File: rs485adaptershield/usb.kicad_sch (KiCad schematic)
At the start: 0 parts

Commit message: more work
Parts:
- added C22, C23, C26: 100n, Capacitor_SMD:C_0603_1608Metric, symbol Device:C
- added C24, C25: 1u, Capacitor_SMD:C_0603_1608Metric, symbol Device:C
- added C4, C6: 100n, Capacitor_SMD:C_0402_1005Metric, symbol Device:C
- added IC1: USB2422-I_MJ, QFN50P400X400X100-25N-D, symbol USB2422-I_MJ:USB2422-I_MJ
- added J1, J5: (no value), Connector_USB:USB_C_Receptacle_GCT_USB4110, symbol Connector:USB_C_Receptacle_USB2.0_16P
- added R14, R15, R16, R9: 5.1k, Capacitor_SMD:C_0402_1005Metric, symbol Device:R
- added U8: AP2171W, Package_TO_SOT_SMD:SOT-23-5, symbol Power_Management:AP2171W
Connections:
- new net: C4.1, J1.SH (SHIELD)
- new net: C6.1, J5.SH (SHIELD)
- new net: J5.A4 (VBUS), J5.A9 (VBUS), J5.B4 (VBUS), J5.B9 (VBUS)
- new net: J1.A4 (VBUS), J1.A9 (VBUS), J1.B4 (VBUS), J1.B9 (VBUS)
- new net +3.3V: C22.2, C23.2, C24.2, IC1.1 (VDD33_1), IC1.18 (VDD33_3), IC1.9 (VDD33_2)
- new net CRFILT: C25.2, IC1.10 (CRFILT)
- new net DA+: J1.A6 (D+), J1.B6 (D+)
- new net DA-: J1.A7 (D-), J1.B7 (D-)
- new net DB+: J5.A6 (D+), J5.B6 (D+)
- new net DB-: J5.A7 (D-), J5.B7 (D-)
- new net GND: C22.1, C23.1, C24.1, C25.1, C26.1, C4.2, C6.2, J1.A1 (GND), J1.A12 (GND), J1.B1 (GND), J1.B12 (GND), J5.A1 (GND), J5.A12 (GND), J5.B1 (GND), J5.B12 (GND), R14.2, R15.2, R16.2, R9.2
- new net PLLFILT: C26.2
- new net USB_CC1A: J1.A5 (CC1), R9.1
- new net USB_CC1B: J5.A5 (CC1), R15.1
- new net USB_CC2A: J1.B5 (CC2), R14.1
- new net USB_CC2B: J5.B5 (CC2), R16.1
- no-connect marks 0 -> 5
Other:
- note added: "1A MAX Silkscreen"
- note added: "pin 1"
- note added: "pin 10"
- note added: "pin 18"
- note added: "pin 23"
- note added: "pin 9"

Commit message: more progress
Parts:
- removed R9: 5.1k, Capacitor_SMD:C_0402_1005Metric, symbol Device:R
- added C27, C28, C29, C30, C33: 100n, Capacitor_SMD:C_0603_1608Metric, symbol Device:C
- added C31, C32: 9n, Capacitor_SMD:C_0603_1608Metric, symbol Device:C
- added D4, D6: LED, LED_SMD:LED_0805_2012Metric, symbol Device:LED
- added R10, R29: 560, Resistor_SMD:R_0805_2012Metric, symbol Device:R
- added R23: 22k, Capacitor_SMD:C_0402_1005Metric, symbol Device:R
- added R26: 12k, Capacitor_SMD:C_0402_1005Metric, symbol Device:R
- added R27, R28: 100k, Capacitor_SMD:C_0402_1005Metric, symbol Device:R
- added R30: 1k, Capacitor_SMD:C_0402_1005Metric, symbol Device:R
- added R31: 2k, Capacitor_SMD:C_0402_1005Metric, symbol Device:R
- added U9: AP2171W, Package_TO_SOT_SMD:SOT-23-5, symbol Power_Management:AP2171W
- added U901, U902: USBLC6-2SC6, Package_TO_SOT_SMD:SOT-23-6, symbol Power_Protection:USBLC6-2SC6
- added Y1: XRCGB24M000F1SBJR0, symbol Device:Crystal
- R14, R15, R16: value 5.1k -> 22k
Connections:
- net PLLFILT is gone; now on net PLL_FILTER: C26.2
- net +3.3V: now also IC1.16 (VBUS_DET), R27.1
- net DA+: now also IC1.3 (USBDP_DN1/PRT_DIS_P1), U901.4 (I/O2); no longer J1.A6 (D+), J1.B6 (D+)
- net DA-: now also IC1.2 (USBDM_DN1/PRT_DIS_M1), U901.6 (I/O1); no longer J1.A7 (D-), J1.B7 (D-)
- net DB+: now also IC1.5 (USBDP_DN2/PRT_DIS_P2), U902.4 (I/O2); no longer J5.A6 (D+), J5.B6 (D+)
- net DB-: now also IC1.4 (USBDM_DN2/PRT_DIS_M2), U902.6 (I/O1); no longer J5.A7 (D-), J5.B7 (D-)
- net GND: now also IC1.25 (EP), U8.2 (GND), C27.1, C28.1, C29.1, C30.1, C31.1, C32.1, C33.1, D4.1 (K), D6.1 (K), R26.2, R28.2, R31.2, U9.2 (GND), U901.2 (GND), U902.2 (GND); no longer R14.2, R15.2, R16.2
- net USB_CC1A: now also R15.1
- net USB_CC1B: now also R23.1; no longer R15.1
- net VBUS_OUT_A: now reaches U8.1 (OUT)
- net VBUS_OUT_A: now also J1.A4 (VBUS), J1.A9 (VBUS), J1.B4 (VBUS), J1.B9 (VBUS), C27.2, R10.1, U901.5 (VBUS)
- net ¬FLG_A: now reaches U8.3 (~{FLG})
- net ¬FLG_A: now also IC1.8 (OCS1_N)
- net EN_A: now reaches U8.4 (EN)
- net EN_A: now also IC1.7 (PRTPWR1/(BC_EN1))
- net VUSB1: now reaches U8.5 (IN)
- net VUSB1: now also R14.2, R15.2, C28.2
- net VBUS_OUT_B: now reaches J5.A4 (VBUS), J5.A9 (VBUS), J5.B4 (VBUS), J5.B9 (VBUS)
- net VBUS_OUT_B: now also C30.2, R29.1, U9.1 (OUT), U902.5 (VBUS)
- net EN_B: now reaches IC1.11 (PRTPWR2)
- net EN_B: now also U9.4 (EN)
- net ¬FLG_B: now reaches IC1.12 (OCS2_N)
- net ¬FLG_B: now also U9.3 (~{FLG})
- net CFG: now reaches IC1.14 (SMBCLK/CFG_SEL0)
- net CFG: now also R28.1
- net ¬RESET: now reaches IC1.15 (RESET_N)
- net ¬RESET: now also C33.2, R27.2, R30.2, R31.1
- net USB_D-: now reaches IC1.19 (USBDM_UP)
- net USB_D+: now reaches IC1.20 (USBDP_UP)
- net XTAL_2: now reaches IC1.21 (XTALOUT/(CLKIN_EN))
- net XTAL_2: now also C31.2, Y1.1
- net XTAL_1: now reaches IC1.22 (XTALIN/CLKIN)
- net XTAL_1: now also C32.2, Y1.2
- net PLL_FILTER: now reaches IC1.23 (PLLFILT)
- net RBIAS: now reaches IC1.24 (RBIAS)
- net RBIAS: now also R26.1
- new net: J1.A7 (D-), J1.B7 (D-), U901.1 (I/O1)
- new net: J1.A6 (D+), J1.B6 (D+), U901.3 (I/O2)
- new net: J5.A7 (D-), J5.B7 (D-), U902.1 (I/O1)
- new net: J5.A6 (D+), J5.B6 (D+), U902.3 (I/O2)
- new net: D4.2 (A), R10.2
- new net: D6.2 (A), R29.2
- new net VUSB2: C29.2, R16.2, R23.2, U9.5 (IN)
- new net ¬USB_HUB_RST: R30.1
- no-connect marks 5 -> 7
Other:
- note added: "1.5A MAX Silkscreen"
- note added: "precision"
- note removed: "1A MAX Silkscreen"
- moved on the sheet: C22, C23, C24, C25, C26, C4, C6, IC1, J1, J5, R14, U8

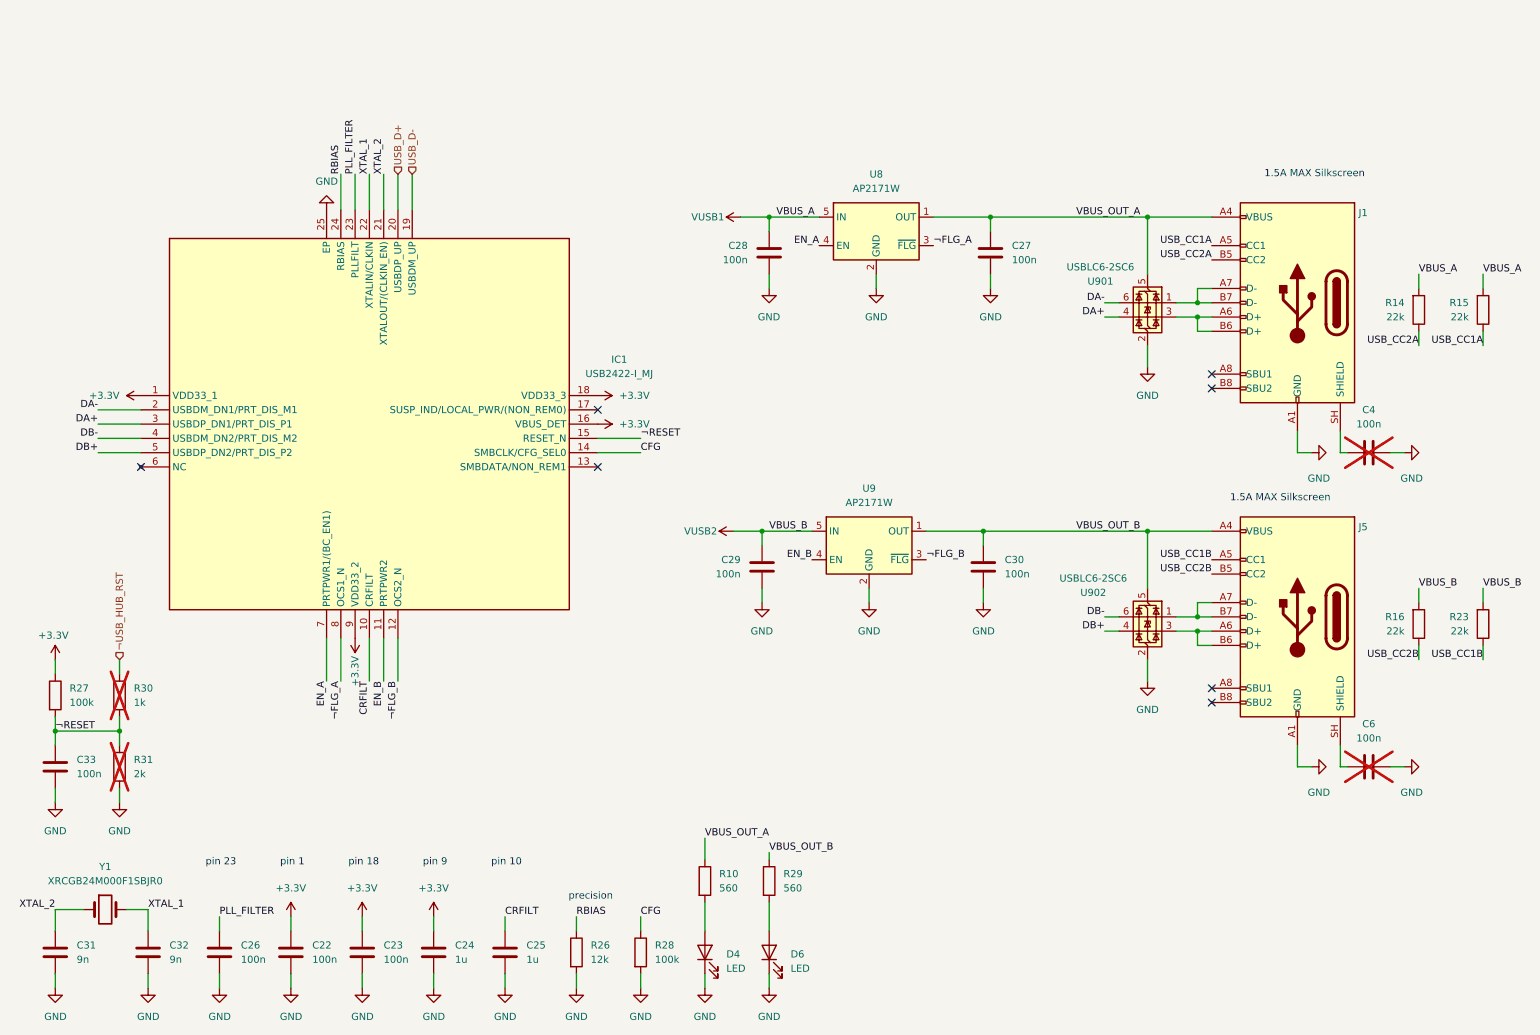
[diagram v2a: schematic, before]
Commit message: schematic mostly finished w/o footprints
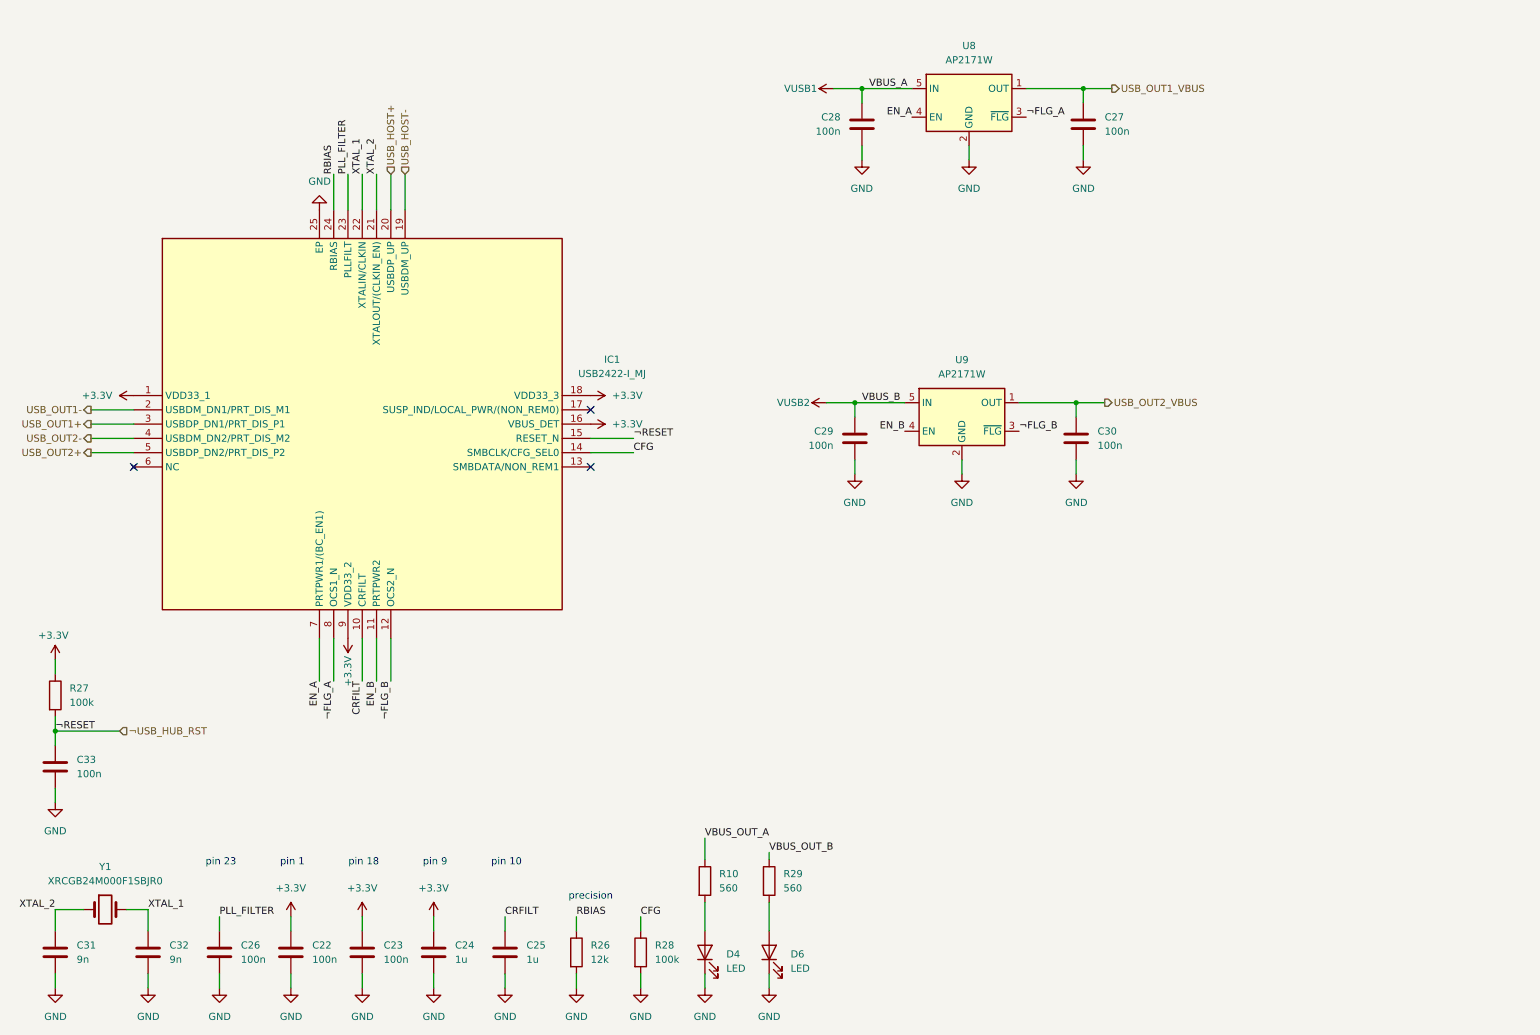
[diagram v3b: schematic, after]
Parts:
- removed C4, C6: 100n, Capacitor_SMD:C_0402_1005Metric, symbol Device:C
- removed J1, J5: (no value), Connector_USB:USB_C_Receptacle_GCT_USB4110, symbol Connector:USB_C_Receptacle_USB2.0_16P
- removed R14, R15, R16, R23: 22k, Capacitor_SMD:C_0402_1005Metric, symbol Device:R
- removed R30: 1k, Capacitor_SMD:C_0402_1005Metric, symbol Device:R
- removed R31: 2k, Capacitor_SMD:C_0402_1005Metric, symbol Device:R
- removed U901, U902: USBLC6-2SC6, Package_TO_SOT_SMD:SOT-23-6, symbol Power_Protection:USBLC6-2SC6
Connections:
- net ¬RESET is gone; now on net ¬USB_HUB_RST: C33.2, IC1.15 (RESET_N), R27.2
- net VBUS_OUT_A: no longer C27.2, U8.1 (OUT)
- net VBUS_OUT_B: no longer C30.2, U9.1 (OUT)
- net DA+ renamed USB_OUT1+
- net DA- renamed USB_OUT1-
- net DB+ renamed USB_OUT2+
- net DB- renamed USB_OUT2-
- net USB_D+ renamed USB_HOST+
- net USB_D- renamed USB_HOST-
- new net USB_OUT1_VBUS: C27.2, U8.1 (OUT)
- new net USB_OUT2_VBUS: C30.2, U9.1 (OUT)
- no-connect marks 7 -> 3
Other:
- note removed: "1.5A MAX Silkscreen"
- moved on the sheet: C27, C28, C29, C30, IC1, U8, U9

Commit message: usb stackup problems
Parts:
- removed C32: 9n, Capacitor_SMD:C_0603_1608Metric, symbol Device:C
- removed Y1: XRCGB24M000F1SBJR0, symbol Device:Crystal
- added TP5: USB_HUB_RST, TestPoint:TestPoint_Pad_D1.0mm, symbol Connector:TestPoint
- added TP6: USB1_VBUS, TestPoint:TestPoint_Pad_D1.0mm, symbol Connector:TestPoint
- added TP7: USB2_VBUS, TestPoint:TestPoint_Pad_D1.0mm, symbol Connector:TestPoint
- added Y1: SG-210STF, Oscillator:Oscillator_SMD_SeikoEpson_SG210-4Pin_2.5x2.0mm, symbol Oscillator:SG-210STF
- C22, C23, C24, C25, C26, C28, C29, C33: footprint Capacitor_SMD:C_0603_1608Metric -> Capacitor_SMD:C_0402_1005Metric
- C27, C30: footprint Capacitor_SMD:C_0603_1608Metric -> Capacitor_SMD:C_0402_1005Metric; now not fitted
- C31: value 9n -> 100n; footprint Capacitor_SMD:C_0603_1608Metric -> Capacitor_SMD:C_0402_1005Metric
- D4, D6: footprint LED_SMD:LED_0805_2012Metric -> LED_SMD:LED_0603_1608Metric
- IC1: footprint QFN50P400X400X100-25N-D -> Package_DFN_QFN:QFN-24-1EP_4x4mm_P0.5mm_EP2.5x2.5mm
- R10, R29: footprint Resistor_SMD:R_0805_2012Metric -> Resistor_SMD:R_0402_1005Metric
- R26, R27, R28: footprint Capacitor_SMD:C_0402_1005Metric -> Resistor_SMD:R_0402_1005Metric
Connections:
- net VBUS_OUT_A is gone; now on net USB_OUT1_VBUS: R10.1
- net VBUS_OUT_B is gone; now on net USB_OUT2_VBUS: R29.1
- net +3.3V: now also C31.2, Y1.1 (~{ST}), Y1.4 (Vcc)
- net GND: now also Y1.2 (GND)
- net USB_OUT1_VBUS: now also TP6.1
- net USB_OUT2_VBUS: now also TP7.1
- net ¬USB_HUB_RST: now also TP5.1
- net XTAL_1 renamed XTAL_IN
- net XTAL_IN: now also Y1.3 (OUT)
- net XTAL_2: no longer names the net of IC1.21 (XTALOUT/(CLKIN_EN))
- net XTAL_2: no longer C31.2
- no-connect marks 3 -> 4
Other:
- moved on the sheet: C22, C23, C24, C25, C26, C33, D4, D6, R10, R26, R27, R28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

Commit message: more layout
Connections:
- net USB_OUT1_VBUS renamed USB_OUT_VBUS_B
- net USB_OUT_VBUS_B: now also R29.1; no longer R10.1
- net USB_OUT2_VBUS renamed USB_OUT_VBUS_A
- net USB_OUT_VBUS_A: now also R10.1; no longer R29.1
- net VUSB1 renamed VUSB_B
- net VUSB2 renamed VUSB_A
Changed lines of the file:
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@@
 		)
 	)
-	(label "VBUS_OUT_A"
+	(label "VBUS_OUT_B"
 		(at 193.04 27.94 0)
 		(effects
@@
 		)
 	)
-	(label "VBUS_OUT_B"
+	(label "VBUS_OUT_A"
 		(at 191.77 83.82 0)
 		(effects
@@
 		)
 	)
-	(label "VBUS_A"
-		(at 165.1 27.94 0)
-		(effects
-			(font
-				(size 1.27 1.27)
-			)
-			(justify left bottom)
-		)
-	)
 	(label "¬FLG_A"
 		(at 193.04 33.02 0)
@@
 		)
 	)
-	(label "VBUS_B"
-		(at 163.83 83.82 0)
-		(effects
-			(font
-				(size 1.27 1.27)
-			)
-			(justify left bottom)
-		)
-	)
 	(label "EN_A"
 		(at 172.72 33.02 180)
@@
 		)
 	)
-	(hierarchical_label "USB_OUT1_VBUS"
+	(hierarchical_label "USB_OUT_VBUS_B"
 		(shape output)
 		(at 223.52 27.94 0)
@@
 		)
 	)
-	(hierarchical_label "USB_OUT2_VBUS"
+	(hierarchical_label "USB_OUT_VBUS_A"
 		(shape output)
 		(at 222.25 83.82 0)
@@
 			)
 		)
-		(property "Value" "VUSB2"
-			(at 151.638 83.82 90)
+		(property "Value" "VUSB_A"
+			(at 148.844 83.82 90)
 			(show_name no)
 			(do_not_autoplace no)
@@
 			)
 		)
-		(property "Value" "VUSB1"
-			(at 152.908 27.94 90)
+		(property "Value" "VUSB_B"
+			(at 150.114 27.94 90)
 			(show_name no)
 			(do_not_autoplace no)
